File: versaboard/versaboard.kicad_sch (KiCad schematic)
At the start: 27 parts, among them J1 UART, J39 Conn_02x20_Odd_Even, J4 DBG, J40 Conn_02x20_Odd_Even, SW1 RST, U1 ATSAML21G18B-AUT, X1 32.768kHz

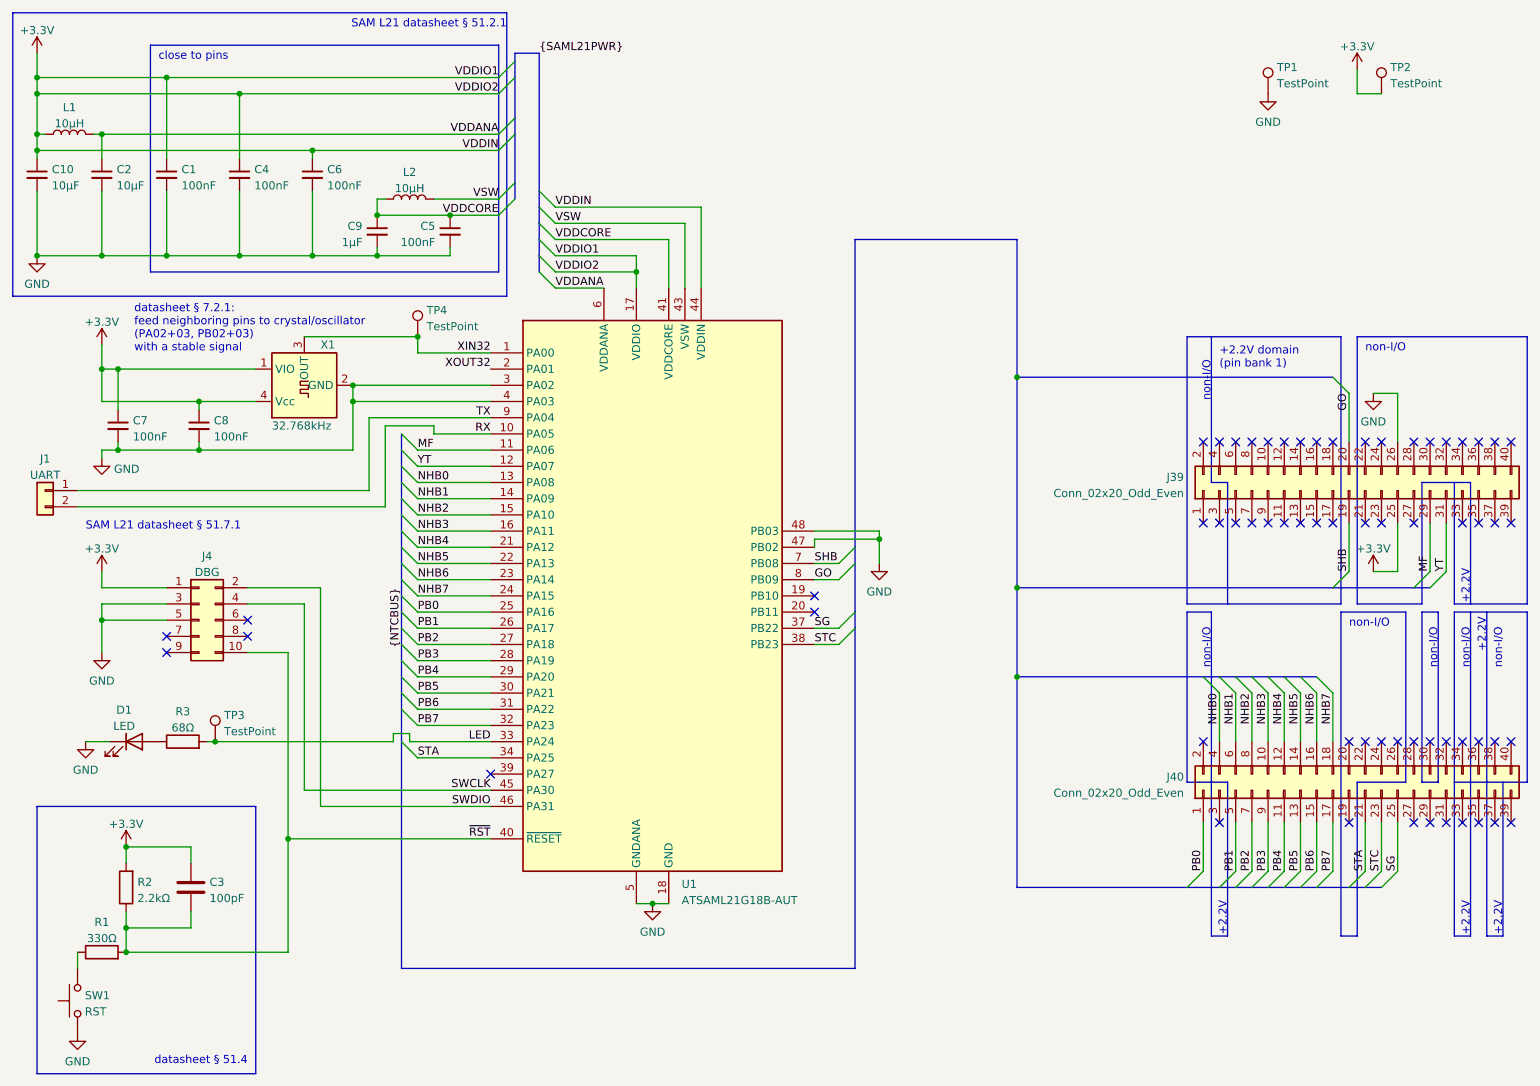
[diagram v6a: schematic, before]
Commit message: versaboard: lead more pins to J40 for potential future use
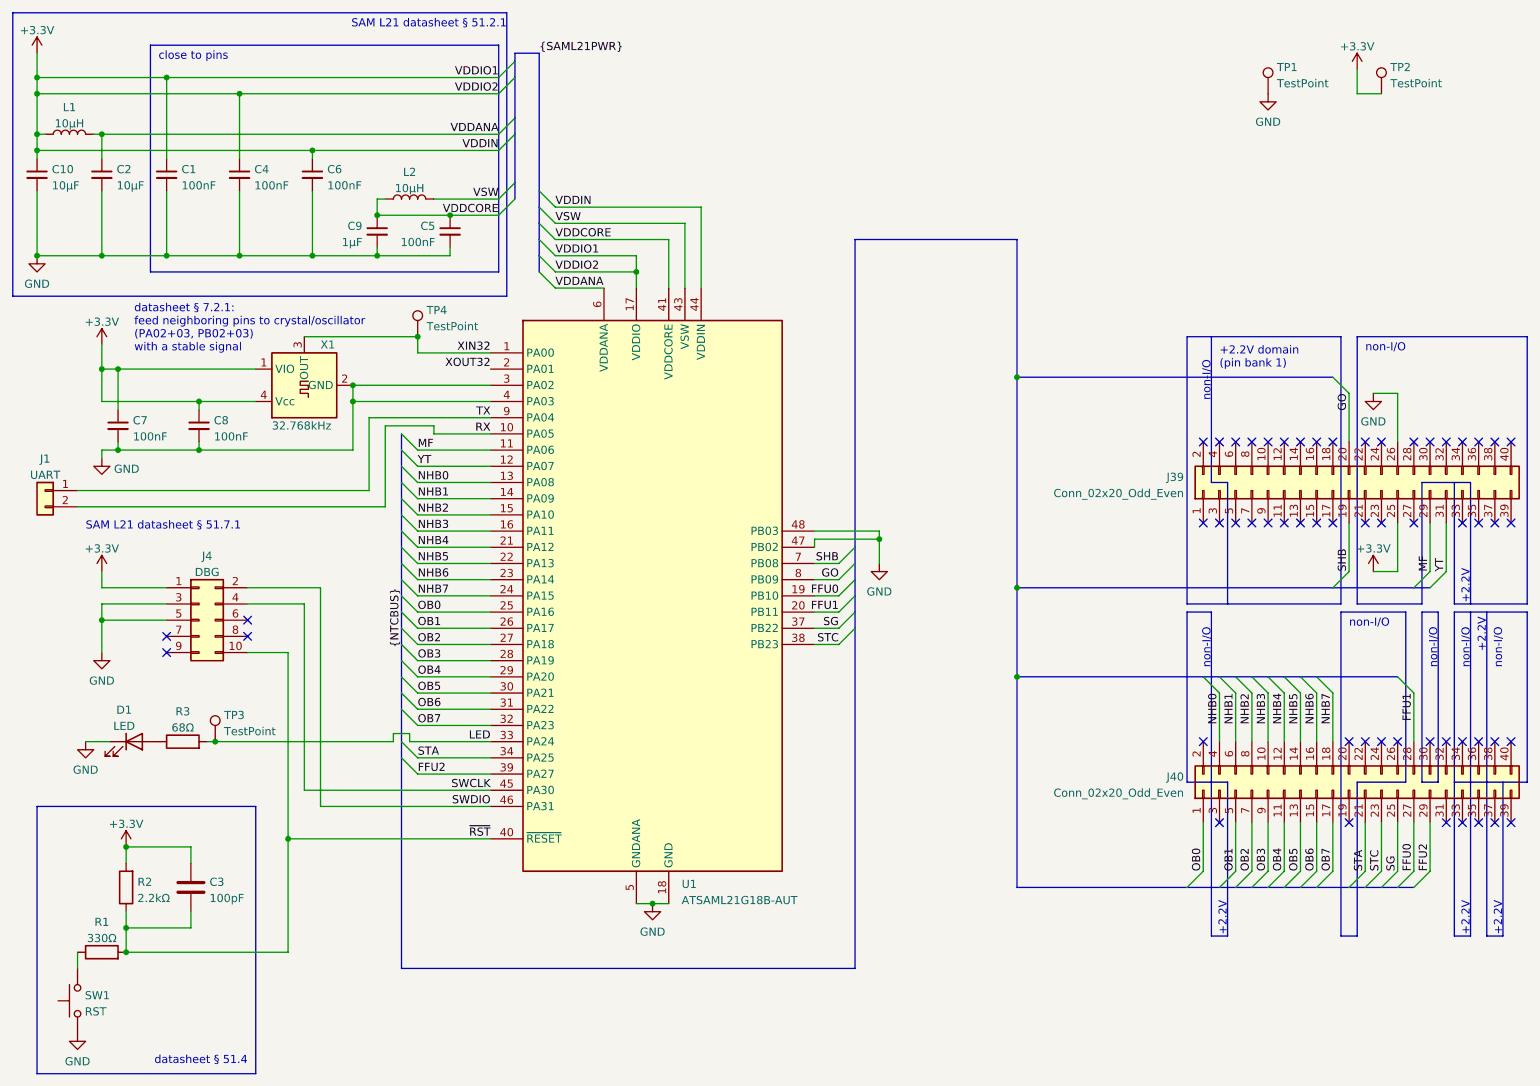
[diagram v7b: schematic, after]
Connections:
- net FFU0: now reaches U1.19 (PB10)
- net FFU0: now also J40.27 (Pin_27)
- net FFU1: now reaches U1.20 (PB11)
- net FFU1: now also J40.28 (Pin_28)
- net FFU2: now reaches U1.39 (PA27)
- net FFU2: now also J40.29 (Pin_29)
- net PB0 renamed OB0
- net PB1 renamed OB1
- net PB2 renamed OB2
- net PB3 renamed OB3
- net PB4 renamed OB4
- net PB5 renamed OB5
- net PB6 renamed OB6
- net PB7 renamed OB7
- no-connect marks 62 -> 56
